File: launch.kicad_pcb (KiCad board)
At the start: 2 copper layers, 301 x 114 mm, 186 parts, among them J0 USB_C_Receptacle_USB2.0, U0 USBLC6-2SC6, U1 ATmega32U4-AU, Y0 16Mhz

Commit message: Add RBG LED matrix
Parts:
- added LA0: WS2812B, LED_SMD:LED_WS2812B_PLCC4_5.0x5.0mm_P3.2mm, B.Cu at (10.0, 5.00)
- added LA1: WS2812B, LED_SMD:LED_WS2812B_PLCC4_5.0x5.0mm_P3.2mm, B.Cu at (160.5, -50.1)
- added LA2: WS2812B, LED_SMD:LED_WS2812B_PLCC4_5.0x5.0mm_P3.2mm, B.Cu at (152.1, -56.7)
- added LA3: WS2812B, LED_SMD:LED_WS2812B_PLCC4_5.0x5.0mm_P3.2mm, B.Cu at (160.5, -43.5)
- added LA4: WS2812B, LED_SMD:LED_WS2812B_PLCC4_5.0x5.0mm_P3.2mm, B.Cu at (152.1, -50.1)
- added LA5: WS2812B, LED_SMD:LED_WS2812B_PLCC4_5.0x5.0mm_P3.2mm, B.Cu at (143.7, -56.7)
- added LB0: WS2812B, LED_SMD:LED_WS2812B_PLCC4_5.0x5.0mm_P3.2mm, B.Cu at (29.0, 5.00)
- added LB1: WS2812B, LED_SMD:LED_WS2812B_PLCC4_5.0x5.0mm_P3.2mm, B.Cu at (152.1, -43.5)
- added LB2: WS2812B, LED_SMD:LED_WS2812B_PLCC4_5.0x5.0mm_P3.2mm, B.Cu at (143.7, -50.1)
- added LB3: WS2812B, LED_SMD:LED_WS2812B_PLCC4_5.0x5.0mm_P3.2mm, B.Cu at (135.2, -56.7)
- added LB4: WS2812B, LED_SMD:LED_WS2812B_PLCC4_5.0x5.0mm_P3.2mm, B.Cu at (126.8, -36.9)
- added LB5: WS2812B, LED_SMD:LED_WS2812B_PLCC4_5.0x5.0mm_P3.2mm, B.Cu at (160.5, -56.7)
- added LC0: WS2812B, LED_SMD:LED_WS2812B_PLCC4_5.0x5.0mm_P3.2mm, B.Cu at (143.7, -43.5)
- added LC1: WS2812B, LED_SMD:LED_WS2812B_PLCC4_5.0x5.0mm_P3.2mm, B.Cu at (135.2, -50.1)
- added LC2: WS2812B, LED_SMD:LED_WS2812B_PLCC4_5.0x5.0mm_P3.2mm, B.Cu at (126.8, -56.7)
- added LC3: WS2812B, LED_SMD:LED_WS2812B_PLCC4_5.0x5.0mm_P3.2mm, B.Cu at (160.5, -23.6)
- added LC4: WS2812B, LED_SMD:LED_WS2812B_PLCC4_5.0x5.0mm_P3.2mm, B.Cu at (152.1, -30.2)
- added LC5: WS2812B, LED_SMD:LED_WS2812B_PLCC4_5.0x5.0mm_P3.2mm, B.Cu at (143.7, -36.9)
- added LD0: WS2812B, LED_SMD:LED_WS2812B_PLCC4_5.0x5.0mm_P3.2mm, B.Cu at (135.2, -43.5)
- added LD1: WS2812B, LED_SMD:LED_WS2812B_PLCC4_5.0x5.0mm_P3.2mm, B.Cu at (126.8, -50.1)
- added LD2: WS2812B, LED_SMD:LED_WS2812B_PLCC4_5.0x5.0mm_P3.2mm, B.Cu at (160.5, -17.0)
- added LD3: WS2812B, LED_SMD:LED_WS2812B_PLCC4_5.0x5.0mm_P3.2mm, B.Cu at (160.5, -30.2)
- added LD4: WS2812B, LED_SMD:LED_WS2812B_PLCC4_5.0x5.0mm_P3.2mm, B.Cu at (152.1, -23.6)
- added LD5: WS2812B, LED_SMD:LED_WS2812B_PLCC4_5.0x5.0mm_P3.2mm, B.Cu at (143.7, -30.2)
- added LE0: WS2812B, LED_SMD:LED_WS2812B_PLCC4_5.0x5.0mm_P3.2mm, B.Cu at (135.2, -36.9)
- added LE1: WS2812B, LED_SMD:LED_WS2812B_PLCC4_5.0x5.0mm_P3.2mm, B.Cu at (126.8, -43.5)
- added LE2: WS2812B, LED_SMD:LED_WS2812B_PLCC4_5.0x5.0mm_P3.2mm, B.Cu at (160.5, -10.4)
- added LE3: WS2812B, LED_SMD:LED_WS2812B_PLCC4_5.0x5.0mm_P3.2mm, B.Cu at (118.4, -50.1)
- added LE4: WS2812B, LED_SMD:LED_WS2812B_PLCC4_5.0x5.0mm_P3.2mm, B.Cu at (152.1, -17.0)
- added LE5: WS2812B, LED_SMD:LED_WS2812B_PLCC4_5.0x5.0mm_P3.2mm, B.Cu at (110.0, -56.7)
- added LF0: WS2812B, LED_SMD:LED_WS2812B_PLCC4_5.0x5.0mm_P3.2mm, B.Cu at (143.7, -23.6)
- added LF1: WS2812B, LED_SMD:LED_WS2812B_PLCC4_5.0x5.0mm_P3.2mm, B.Cu at (152.1, -36.9)
- added LF2: WS2812B, LED_SMD:LED_WS2812B_PLCC4_5.0x5.0mm_P3.2mm, B.Cu at (118.4, -56.7)
- added LF3: WS2812B, LED_SMD:LED_WS2812B_PLCC4_5.0x5.0mm_P3.2mm, B.Cu at (118.4, -43.5)
- added LF4: WS2812B, LED_SMD:LED_WS2812B_PLCC4_5.0x5.0mm_P3.2mm, B.Cu at (152.1, -10.4)
- added LG0: WS2812B, LED_SMD:LED_WS2812B_PLCC4_5.0x5.0mm_P3.2mm, B.Cu at (110.0, -50.1)
- added LG1: WS2812B, LED_SMD:LED_WS2812B_PLCC4_5.0x5.0mm_P3.2mm, B.Cu at (143.7, -17.0)
- added LG2: WS2812B, LED_SMD:LED_WS2812B_PLCC4_5.0x5.0mm_P3.2mm, B.Cu at (101.6, -56.7)
- added LG3: WS2812B, LED_SMD:LED_WS2812B_PLCC4_5.0x5.0mm_P3.2mm, B.Cu at (135.2, -23.6)
- added LG4: WS2812B, LED_SMD:LED_WS2812B_PLCC4_5.0x5.0mm_P3.2mm, B.Cu at (126.8, -30.2)
- added LG5: WS2812B, LED_SMD:LED_WS2812B_PLCC4_5.0x5.0mm_P3.2mm, B.Cu at (118.4, -36.9)
- added LH0: WS2812B, LED_SMD:LED_WS2812B_PLCC4_5.0x5.0mm_P3.2mm, B.Cu at (110.0, -43.5)
- added LH1: WS2812B, LED_SMD:LED_WS2812B_PLCC4_5.0x5.0mm_P3.2mm, B.Cu at (110.0, -10.4)
- added LH2: WS2812B, LED_SMD:LED_WS2812B_PLCC4_5.0x5.0mm_P3.2mm, B.Cu at (101.6, -50.1)
- added LH3: WS2812B, LED_SMD:LED_WS2812B_PLCC4_5.0x5.0mm_P3.2mm, B.Cu at (135.2, -17.0)
- added LH4: WS2812B, LED_SMD:LED_WS2812B_PLCC4_5.0x5.0mm_P3.2mm, B.Cu at (93.2, -56.7)
- added LH5: WS2812B, LED_SMD:LED_WS2812B_PLCC4_5.0x5.0mm_P3.2mm, B.Cu at (126.8, -23.6)
- added LI0: WS2812B, LED_SMD:LED_WS2812B_PLCC4_5.0x5.0mm_P3.2mm, B.Cu at (118.4, -30.2)
- added LI1: WS2812B, LED_SMD:LED_WS2812B_PLCC4_5.0x5.0mm_P3.2mm, B.Cu at (110.0, -36.9)
- added LI2: WS2812B, LED_SMD:LED_WS2812B_PLCC4_5.0x5.0mm_P3.2mm, B.Cu at (101.6, -43.5)
- added LI3: WS2812B, LED_SMD:LED_WS2812B_PLCC4_5.0x5.0mm_P3.2mm, B.Cu at (135.2, -10.4)
- added LI4: WS2812B, LED_SMD:LED_WS2812B_PLCC4_5.0x5.0mm_P3.2mm, B.Cu at (93.2, -50.1)
- added LI5: WS2812B, LED_SMD:LED_WS2812B_PLCC4_5.0x5.0mm_P3.2mm, B.Cu at (101.6, -17.0)
- added LJ0: WS2812B, LED_SMD:LED_WS2812B_PLCC4_5.0x5.0mm_P3.2mm, B.Cu at (143.7, -10.4)
- added LJ1: WS2812B, LED_SMD:LED_WS2812B_PLCC4_5.0x5.0mm_P3.2mm, B.Cu at (118.4, -23.6)
- added LJ2: WS2812B, LED_SMD:LED_WS2812B_PLCC4_5.0x5.0mm_P3.2mm, B.Cu at (110.0, -30.2)
- added LJ3: WS2812B, LED_SMD:LED_WS2812B_PLCC4_5.0x5.0mm_P3.2mm, B.Cu at (101.6, -36.9)
- added LJ4: WS2812B, LED_SMD:LED_WS2812B_PLCC4_5.0x5.0mm_P3.2mm, B.Cu at (93.2, -43.5)
- added LJ5: WS2812B, LED_SMD:LED_WS2812B_PLCC4_5.0x5.0mm_P3.2mm, B.Cu at (126.8, -10.4)
- added LK0: WS2812B, LED_SMD:LED_WS2812B_PLCC4_5.0x5.0mm_P3.2mm, B.Cu at (84.7, -50.1)
- added LK1: WS2812B, LED_SMD:LED_WS2812B_PLCC4_5.0x5.0mm_P3.2mm, B.Cu at (118.4, -17.0)
- added LK2: WS2812B, LED_SMD:LED_WS2812B_PLCC4_5.0x5.0mm_P3.2mm, B.Cu at (76.3, -56.7)
- added LK3: WS2812B, LED_SMD:LED_WS2812B_PLCC4_5.0x5.0mm_P3.2mm, B.Cu at (110.0, -23.6)
- added LK4: WS2812B, LED_SMD:LED_WS2812B_PLCC4_5.0x5.0mm_P3.2mm, B.Cu at (126.8, -17.0)
- added LK5: WS2812B, LED_SMD:LED_WS2812B_PLCC4_5.0x5.0mm_P3.2mm, B.Cu at (93.2, -36.9)
- added LL0: WS2812B, LED_SMD:LED_WS2812B_PLCC4_5.0x5.0mm_P3.2mm, B.Cu at (84.7, -43.5)
- added LL1: WS2812B, LED_SMD:LED_WS2812B_PLCC4_5.0x5.0mm_P3.2mm, B.Cu at (118.4, -10.4)
- added LL2: WS2812B, LED_SMD:LED_WS2812B_PLCC4_5.0x5.0mm_P3.2mm, B.Cu at (76.3, -50.1)
- added LL3: WS2812B, LED_SMD:LED_WS2812B_PLCC4_5.0x5.0mm_P3.2mm, B.Cu at (110.0, -17.0)
- added LL4: WS2812B, LED_SMD:LED_WS2812B_PLCC4_5.0x5.0mm_P3.2mm, B.Cu at (101.6, -23.6)
- added LL5: WS2812B, LED_SMD:LED_WS2812B_PLCC4_5.0x5.0mm_P3.2mm, B.Cu at (93.2, -30.2)
- added LM0: WS2812B, LED_SMD:LED_WS2812B_PLCC4_5.0x5.0mm_P3.2mm, B.Cu at (84.7, -36.9)
- added LM1: WS2812B, LED_SMD:LED_WS2812B_PLCC4_5.0x5.0mm_P3.2mm, B.Cu at (76.3, -43.5)
- added LM2: WS2812B, LED_SMD:LED_WS2812B_PLCC4_5.0x5.0mm_P3.2mm, B.Cu at (84.7, -56.7)
- added LM3: WS2812B, LED_SMD:LED_WS2812B_PLCC4_5.0x5.0mm_P3.2mm, B.Cu at (101.6, -30.2)
- added LM4: WS2812B, LED_SMD:LED_WS2812B_PLCC4_5.0x5.0mm_P3.2mm, B.Cu at (93.2, -23.6)
- added LM5: WS2812B, LED_SMD:LED_WS2812B_PLCC4_5.0x5.0mm_P3.2mm, B.Cu at (84.7, -30.2)
- added LN0: WS2812B, LED_SMD:LED_WS2812B_PLCC4_5.0x5.0mm_P3.2mm, B.Cu at (76.3, -36.9)
- added LN1: WS2812B, LED_SMD:LED_WS2812B_PLCC4_5.0x5.0mm_P3.2mm, B.Cu at (101.6, -10.4)
- added LN2: WS2812B, LED_SMD:LED_WS2812B_PLCC4_5.0x5.0mm_P3.2mm, B.Cu at (93.2, -17.0)
- added LO0: WS2812B, LED_SMD:LED_WS2812B_PLCC4_5.0x5.0mm_P3.2mm, B.Cu at (84.7, -23.6)
- added LO1: WS2812B, LED_SMD:LED_WS2812B_PLCC4_5.0x5.0mm_P3.2mm, B.Cu at (76.3, -30.2)
- added LO2: WS2812B, LED_SMD:LED_WS2812B_PLCC4_5.0x5.0mm_P3.2mm, B.Cu at (93.2, -10.4)
- added LO3: WS2812B, LED_SMD:LED_WS2812B_PLCC4_5.0x5.0mm_P3.2mm, B.Cu at (84.7, -17.0)
- moved R0 75.5 mm to (222.8, -35.5), turned to 270 degrees
- moved C4 19.3 mm to (224.5, -20.2), turned to 0 degrees
- moved C2 4.96 mm to (194.5, -17.0)
- moved C0 3.83 mm to (197.2, -21.5)
- moved C1 3.70 mm to (202.0, -23.5)

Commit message: Route LEDs
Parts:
- LA0, LA1, LA2, LA3, LA4, LA5, LB0, LB1, LB2, LB3, LB4, LB5, LC0, LC1, LC2, LC3, LC4, LC5, LD0, LD1, LD2, LD3, LD4, LD5, LE0, LE1, LE2, LE3, LE4, LE5, LF0, LF1, LF2, LF3, LF4, LG0, LG1, LG2, LG3, LG4, LG5, LH0, LH1, LH2, LH3, LH4, LH5, LI0, LI1, LI2, LI3, LI4, LI5, LJ0, LJ1, LJ2, LJ3, LJ4, LJ5, LK0, LK1, LK2, LK3, LK4, LK5, LL0, LL1, LL2, LL3, LL4, LL5, LM0, LM1, LM2, LM3, LM4, LM5, LN0, LN1, LN2, LO0, LO1, LO2, LO3, SWA0, SWA1, SWA2, SWA3, SWA4, SWA5, SWB0, SWB1, SWB2, SWB3, SWB4, SWB5, SWC0, SWC1, SWC2, SWC3, SWC4, SWC5, SWD0, SWD1, SWD2, SWD3, SWD4, SWD5, SWE0, SWE1, SWE2, SWE3, SWE4, SWE5, SWF0, SWF1, SWF2, SWF3, SWF4, SWG0, SWG1, SWG2, SWG3, SWG4, SWG5, SWH0, SWH1, SWH2, SWH3, SWH4, SWH5, SWI0, SWI1, SWI2, SWI3, SWI4, SWI5, SWJ0, SWJ1, SWJ2, SWJ3, SWJ4, SWJ5, SWK0, SWK1, SWK2, SWK3, SWK4, SWK5, SWL0, SWL1, SWL2, SWL3, SWL4, SWL5, SWM0, SWM1, SWM2, SWM3, SWM4, SWM5, SWN0, SWN1, SWN2, SWO0, SWO1, SWO2, SWO3: moved to F.Cu
- moved LM5 243.3 mm to (290.2, 100.0)
- moved LO1 220.7 mm to (290.2, 24.0)
- moved LL5 220.6 mm to (271.2, 100.0)
- moved LO3 220.2 mm to (290.2, 62.0)
- moved LK5 209.9 mm to (252.2, 100.0)
- moved LO0 207.5 mm to (290.2, 5.00)
- moved LM4 206.6 mm to (271.2, 81.0)
- moved LO2 204.2 mm to (290.2, 43.0)
- moved LA5 200.0 mm to (19.5, 100.0)
- moved LB5 195.7 mm to (43.2, 100.0)
- moved LM2 190.9 mm to (247.5, 43.0)
- moved LN0 190.1 mm to (261.8, 5.00)
- moved LN2 183.4 mm to (266.5, 43.0)
- moved LA4 183.1 mm to (24.2, 81.0)
- moved LM3 180.7 mm to (257.0, 62.0)
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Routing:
- net GND: track 0.00 -> 3339.9 mm, vias 0 -> 99
- net VCC: track 0.00 -> 2770.0 mm, vias 0 -> 99
- net Net-(LA2-Pad4): track 0.00 -> 342.7 mm
- net Net-(LA1-Pad4): track 0.00 -> 339.9 mm
- net Net-(LA3-Pad4): track 0.00 -> 338.0 mm
- net Net-(LA4-Pad4): track 0.00 -> 301.3 mm
- net Net-(LA5-Pad4): track 0.00 -> 287.0 mm
- net ROW2: track 275.8 -> 318.6 mm, vias 0 -> 15
- net ROW1: track 280.5 -> 323.4 mm, vias 0 -> 15
- net ROW0: track 280.5 -> 323.4 mm, vias 0 -> 15
- net ROW3: track 271.0 -> 311.0 mm, vias 0 -> 14
- net ROW4: track 247.0 -> 284.4 mm, vias 0 -> 13
- net Net-(LE5-Pad2): track 0.00 -> 34.9 mm
- net ROW5: track 270.8 -> 305.2 mm, vias 0 -> 12
- net Net-(LM3-Pad2): track 0.00 -> 30.1 mm
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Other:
- board size 301 x 114 mm -> 305.2 x 120 mm

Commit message: Route rows to EC
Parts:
- moved R4 86.7 mm to (141.2, -5.95), turned to 270 degrees
- moved R3 82.0 mm to (141.2, -27.5), turned to 270 degrees
- moved C4 73.8 mm to (151.2, -29.5)
- moved J0 73.8 mm to (145.2, -53.2)
- moved R0 73.8 mm to (149.5, -44.8)
- moved R1 73.8 mm to (142.2, -44.8)
- moved U0 73.8 mm to (145.8, -41.5)
- moved U1 73.4 mm to (145.2, -16.8), turned to 270 degrees
- moved C3 72.4 mm to (135.2, -20.4), turned to 270 degrees
- moved D0 71.5 mm to (147.5, -27.5), turned to 270 degrees
- moved R2 69.9 mm to (143.2, -27.5), turned to 90 degrees
- moved C7 65.6 mm to (145.5, -27.5), turned to 90 degrees
- moved Y0 61.6 mm to (155.8, -17.1), turned to 270 degrees
- moved C6 60.0 mm to (159.8, -19.6), turned to 0 degrees
- moved C2 59.5 mm to (135.2, -13.2)
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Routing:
- net ROW5: track 305.2 -> 579.2 mm, vias 12 -> 14
- net ROW4: track 284.4 -> 556.2 mm, vias 13 -> 17
- net ROW3: track 311.0 -> 545.6 mm, vias 14 -> 16
- net ROW2: track 318.6 -> 530.7 mm, vias 15 -> 17
- net ROW1: track 323.4 -> 510.5 mm, vias 15 -> 17
- net COLA: track 104.9 -> 252.3 mm
- net COLO: track 57.0 -> 202.9 mm
- net ROW0: track 323.4 -> 461.7 mm, vias 15 -> 16
- net COLB: track 109.9 -> 237.6 mm
- net Net-(LA0-Pad4): track 8.86 -> 131.8 mm, vias 0 -> 2
- net COLN: track 40.0 -> 156.6 mm
- net COLC: track 114.2 -> 222.1 mm
- net COLM: track 133.2 -> 225.3 mm
- net COLD: track 114.2 -> 202.4 mm
- net COLL: track 133.2 -> 205.5 mm
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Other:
- board size 305.2 x 120 mm -> 305.2 x 160 mm
- net class Default: clearance 0.2 -> 0.1
- rule trace_clearance: 0.2 -> 0.1

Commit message: Connect everything in schematic
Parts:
- added C8: 0.1uF, Capacitor_SMD:C_0805_2012Metric, B.Cu at (140.2, -27.5)
- moved R1 45.3 mm to (175.8, -14.2), turned to 0 degrees
- moved J0 38.9 mm to (170.0, -23.2)
- moved R0 38.7 mm to (176.5, -17.0)
- moved U0 37.4 mm to (170.0, -13.0)
- moved D0 30.1 mm to (170.0, -7.50), turned to 0 degrees
- moved C4 26.0 mm to (166.5, -8.45), turned to 90 degrees
- moved C0 1.59 mm to (149.2, -8.21), turned to 90 degrees
- moved C2 1.52 mm to (136.6, -12.8), turned to 180 degrees
- moved C3 1.52 mm to (136.6, -20.8), turned to 180 degrees
- moved C1 1.10 mm to (155.3, -21.6), turned to 0 degrees
- moved R2 1.00 mm to (144.2, -27.5)
- moved R3 1.00 mm to (142.2, -27.5)
- moved C7 0.80 mm to (146.3, -27.5)
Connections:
- net Net-(J0-PadA6) renamed /DIN+
- net Net-(J0-PadA7) renamed /DIN-
- net Net-(R2-Pad2) renamed /DOUT+
- net Net-(R3-Pad1) renamed /DOUT-
- D0 pad 2: Net-(D0-Pad2) -> /VBUS
- J0 pad A4: Net-(D0-Pad2) -> /VBUS
- J0 pad A9: Net-(D0-Pad2) -> /VBUS
- J0 pad B4: Net-(D0-Pad2) -> /VBUS
- J0 pad B9: Net-(D0-Pad2) -> /VBUS
- U0 pad 5: Net-(D0-Pad2) -> /VBUS
- U1 pad 7: Net-(D0-Pad2) -> VCC
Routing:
- net VCC: track 2782.6 -> 2902.4 mm, vias 99 -> 100
- net GND: track 3350.6 -> 3428.8 mm, vias 99 -> 113
- net /DOUT-: track 0.00 -> 45.4 mm, vias 0 -> 2
- net COLJ: track 154.5 -> 199.2 mm, vias 0 -> 2
- net /DOUT+: track 0.00 -> 43.6 mm, vias 0 -> 2
- net COLF: track 140.0 -> 175.5 mm, vias 0 -> 2
- net COLE: track 178.7 -> 211.6 mm, vias 0 -> 2
- net COLD: track 202.4 -> 232.4 mm, vias 0 -> 2
- net COLA: track 252.3 -> 279.6 mm, vias 0 -> 2
- net COLC: track 222.1 -> 249.4 mm, vias 0 -> 2
- net COLN: track 156.6 -> 183.3 mm, vias 0 -> 2
- net COLB: track 237.6 -> 264.2 mm, vias 0 -> 2
- net COLG: track 139.2 -> 164.5 mm, vias 0 -> 2
- net /VBUS: track 0.00 -> 25.2 mm, vias 0 -> 1
- net COLK: track 185.5 -> 210.4 mm, vias 0 -> 2
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- added copper zone on B.Cu, net GND

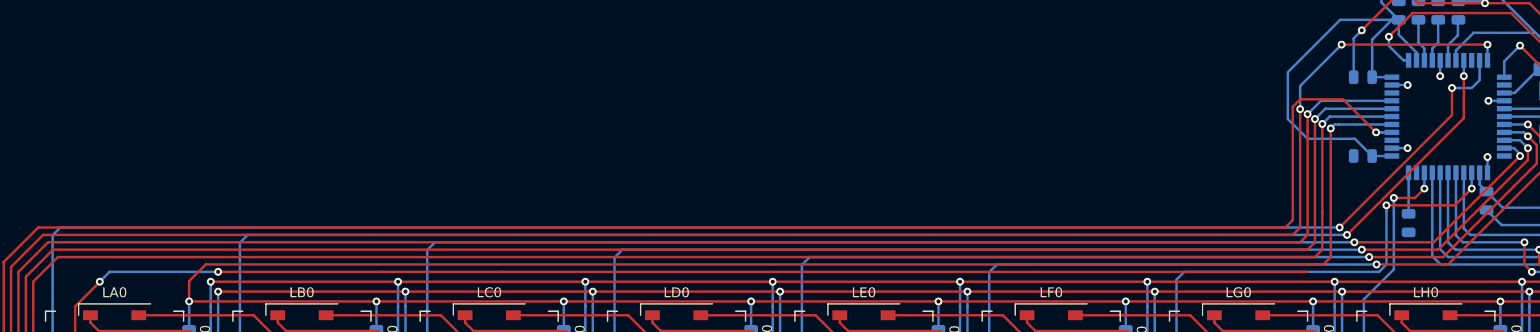
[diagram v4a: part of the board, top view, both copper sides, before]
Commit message: Route LED data in to EC
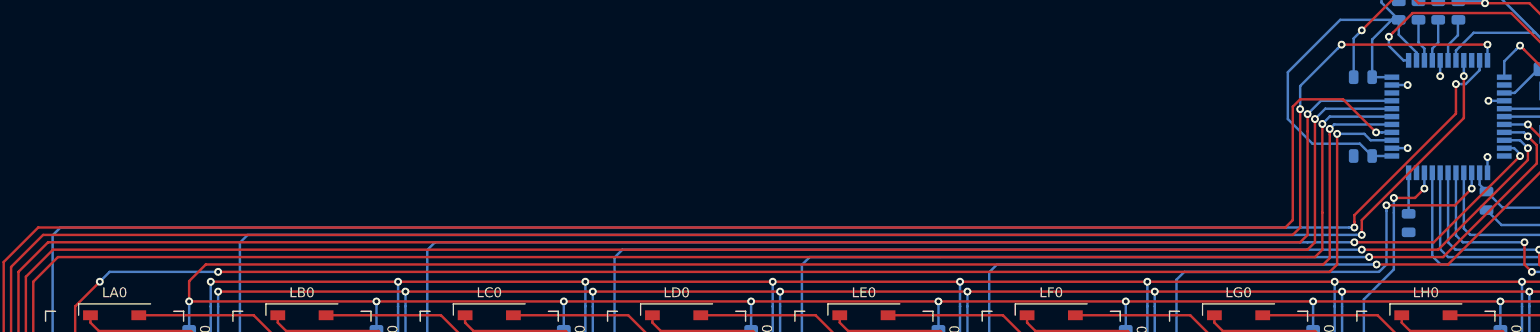
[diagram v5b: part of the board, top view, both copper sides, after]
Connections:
- LA0 pad 4: Net-(LA0-Pad4) -> LED
- U1 pad 36: Net-(U1-Pad36) -> LED
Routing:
- net LED: track 0.00 -> 154.2 mm, vias 0 -> 3
- net Net-(LA0-Pad4): track 131.8 -> 0.00 mm, vias 2 -> 0
- net COLB: track 264.2 -> 265.1 mm
- net COLA: track 279.6 -> 280.4 mm

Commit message: Reduce board size
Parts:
- removed C8: 0.1uF, Capacitor_SMD:C_0805_2012Metric
- R2, R3: moved to F.Cu
- U1: value ATmega32U4-AU -> ATmega32U4-MU; footprint Package_QFP:TQFP-44_10x10mm_P0.8mm -> Package_DFN_QFN:QFN-44-1EP_7x7mm_P0.5mm_EP5.2x5.2mm
- moved C1 23.3 mm to (142.8, -2.00)
- moved R2 19.0 mm to (138.0, -9.56), turned to 270 degrees
- moved R3 19.0 mm to (136.0, -9.56), turned to 90 degrees
- moved J0 16.1 mm to (160.2, -10.5)
- moved C7 15.4 mm to (140.0, -13.5), turned to 0 degrees
- moved C6 13.0 mm to (151.2, -9.75)
- moved C5 12.7 mm to (151.2, -5.25)
- moved Y0 12.7 mm to (147.5, -7.50)
- moved U1 11.8 mm to (138.2, -7.25)
- moved C4 11.6 mm to (178.0, -7.00), turned to 180 degrees
- moved C3 11.2 mm to (133.0, -10.2), turned to 270 degrees
- moved R1 10.8 mm to (185.8, -10.2)
- moved C2 9.75 mm to (132.3, -4.00)
- moved R4 9.57 mm to (133.1, -1.00), turned to 180 degrees
- moved R0 7.27 mm to (179.8, -10.5)
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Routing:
- net GND: track 3428.8 -> 273.9 mm, vias 113 -> 91
- net VCC: track 2902.4 -> 249.2 mm, vias 100 -> 89
- net ROW0: track 461.7 -> 338.1 mm
- net ROW1: track 510.5 -> 390.9 mm
- net ROW2: track 530.7 -> 430.3 mm
- net ROW3: track 545.6 -> 465.0 mm
- net ROW4: track 556.2 -> 476.7 mm, vias 17 -> 14
- net ROW5: track 579.2 -> 540.0 mm
- net Net-(LA2-Pad4): track 342.7 -> 310.8 mm
- net Net-(LA3-Pad4): track 338.0 -> 306.0 mm
- net COLJ: track 199.2 -> 168.9 mm
- net /VBUS: track 25.2 -> 0.00 mm, vias 1 -> 0
- net /DOUT-: track 45.4 -> 20.3 mm, vias 2 -> 0
- net Net-(LA1-Pad4): track 339.9 -> 315.5 mm
- net /DOUT+: track 43.6 -> 19.5 mm, vias 2 -> 0
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- added copper zone on In2.Cu, net GND
- added copper zone on In1.Cu, net VCC
- removed copper zone on B.Cu, net GND
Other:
- board size 305.2 x 160 mm -> 298.2 x 128.8 mm
- copper layers 2 -> 4

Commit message: Reroute to remove space at top of board
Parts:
- added D1: D, Diode_SMD:D_0805_2012Metric, B.Cu at (280.2, 16.8)
- R2, R3: moved to B.Cu
- moved C2 188.3 mm to (294.2, 92.0), turned to 0 degrees
- moved R4 187.1 mm to (294.2, 94.0), turned to 0 degrees
- moved C3 185.2 mm to (294.2, 81.0), turned to 0 degrees
- moved C0 180.8 mm to (294.2, 90.0), turned to 180 degrees
- moved U1 176.3 mm to (288.0, 85.8)
- moved C7 175.9 mm to (289.8, 78.8), turned to 90 degrees
- moved Y0 173.9 mm to (294.5, 85.5)
- moved R2 173.9 mm to (287.8, 78.8), turned to 90 degrees
- moved R3 173.9 mm to (285.8, 78.8), turned to 270 degrees
- moved C6 173.6 mm to (297.5, 83.8), turned to 90 degrees
- moved C5 173.0 mm to (297.5, 87.2), turned to 270 degrees
- moved C1 171.8 mm to (294.2, 79.0)
- moved C4 136.1 mm to (283.8, 78.8), turned to 90 degrees
- moved J0 117.9 mm to (277.0, 6.00)
- moved U0 110.8 mm to (277.0, 15.2)
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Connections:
- U1 pad 1: COLJ -> Net-(U1-Pad1)
- U1 pad 10: COLA -> COLO
- U1 pad 11: ROW4 -> COLN
- U1 pad 12: COLN -> Net-(U1-Pad12)
- U1 pad 18: COLF -> COLM
- U1 pad 19: COLE -> COLL
- U1 pad 20: COLD -> COLK
- U1 pad 21: COLC -> COLJ
- U1 pad 22: Net-(U1-Pad22) -> COLI
- U1 pad 25: COLG -> COLH
- U1 pad 26: COLO -> COLG
- U1 pad 27: COLI -> COLF
- U1 pad 28: COLK -> COLE
- U1 pad 29: COLL -> COLD
- U1 pad 30: COLM -> COLC
- U1 pad 31: COLH -> COLB
- U1 pad 32: Net-(U1-Pad32) -> COLA
- U1 pad 36: LED -> ROW5
- U1 pad 37: ROW5 -> ROW4
- U1 pad 38: ROW0 -> ROW3
- U1 pad 39: ROW1 -> ROW2
- U1 pad 40: ROW2 -> ROW1
- U1 pad 41: ROW3 -> ROW0
- U1 pad 8: COLB -> Net-(U1-Pad8)
- U1 pad 9: Net-(U1-Pad9) -> LED
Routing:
- net LED: track 140.6 -> 356.4 mm
- net COLO: track 226.7 -> 72.1 mm, vias 2 -> 0
- net ROW5: track 540.0 -> 395.7 mm
- net ROW4: track 476.7 -> 353.2 mm, vias 14 -> 13
- net COLH: track 134.7 -> 257.3 mm, vias 0 -> 2
- net COLA: track 257.9 -> 379.5 mm, vias 1 -> 2
- net COLG: track 151.5 -> 270.6 mm
- net COLB: track 243.5 -> 357.5 mm, vias 1 -> 2
- net COLF: track 161.3 -> 268.2 mm
- net COLC: track 235.5 -> 341.7 mm
- net COLD: track 218.2 -> 324.0 mm
- net COLE: track 197.3 -> 301.5 mm
- net COLM: track 246.6 -> 154.3 mm
- net COLI: track 150.9 -> 241.8 mm
- net ROW3: track 465.0 -> 381.8 mm, vias 16 -> 14
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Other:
- board size 298.2 x 128.8 mm -> 298.2 x 113 mm
- net class Default: via_dia 0.8 -> 0.4; via_drill 0.4 -> 0.2
- rule via_min_drill: 0.3 -> 0.2
